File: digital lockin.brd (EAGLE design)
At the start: 76.2 x 94.9 mm, 24 parts, among them IC1 OPA2650E, IC2 LM358D, T2 NPN, U2 RASPBERRY_PICOSMD-TH, U5 TL431AIDBZR

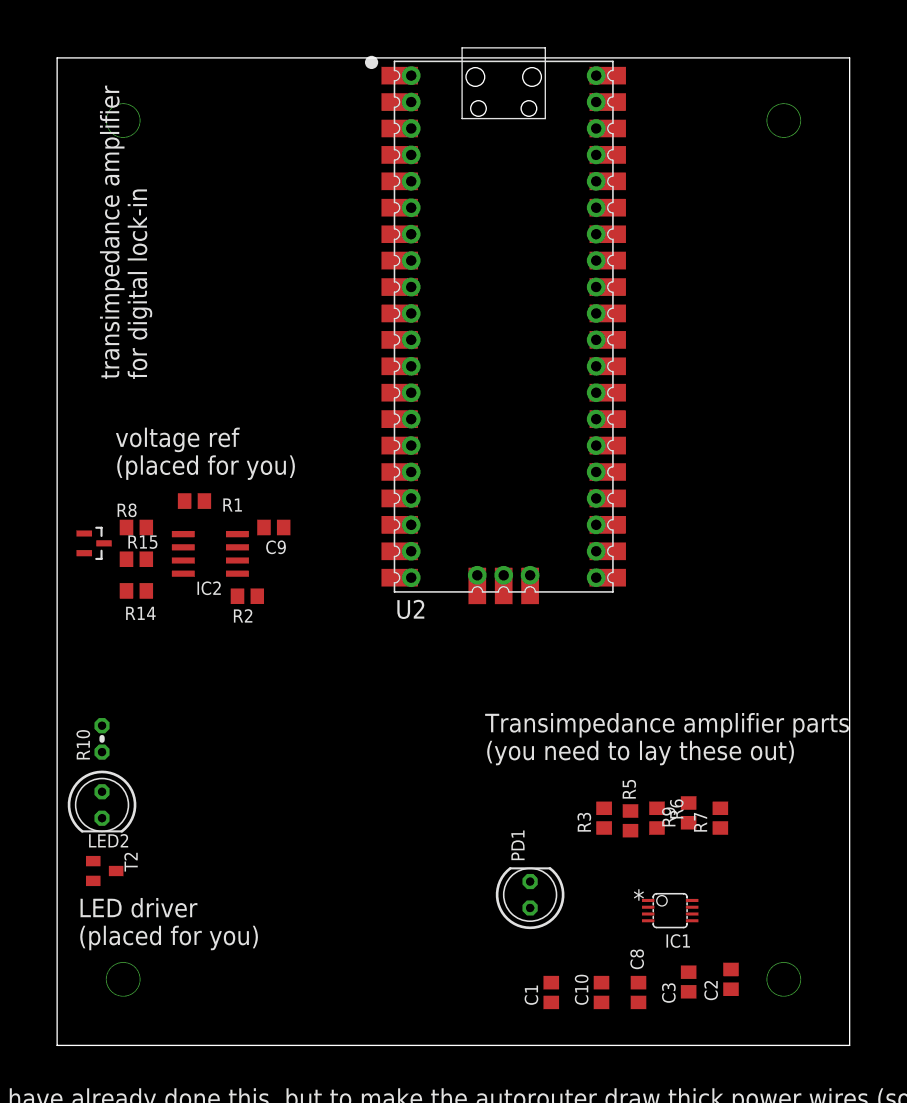
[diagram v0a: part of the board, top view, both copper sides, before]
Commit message: Lab 3 lock-in amplifier
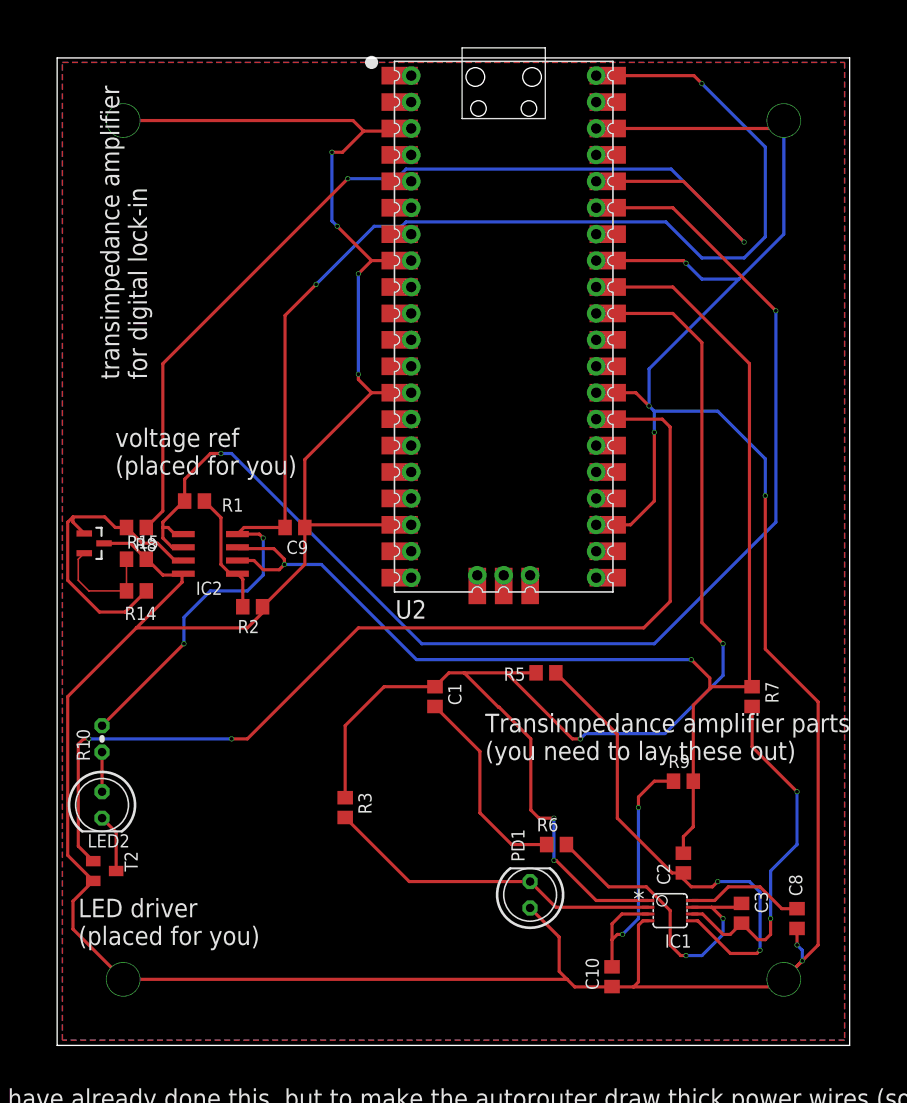
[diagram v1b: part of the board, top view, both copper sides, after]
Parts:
- moved C1 30.6 mm to (36.3, 33.5), turned to 270 degrees
- moved R3 24.9 mm to (27.7, 22.9), turned to 90 degrees
- moved C8 16.8 mm to (71.1, 12.2)
- moved R5 16.4 mm to (47.0, 35.8), turned to 0 degrees
- moved C2 12.1 mm to (60.2, 17.5)
- moved R7 12.1 mm to (66.8, 33.5), turned to 90 degrees
- moved R6 9.98 mm to (48.0, 19.3), turned to 0 degrees
- moved C3 8.33 mm to (65.8, 12.7), turned to 90 degrees
- moved R9 3.09 mm to (60.2, 25.4), turned to 180 degrees
- moved C9 2.03 mm to (22.9, 49.8)
- moved C10 1.83 mm to (53.3, 6.60)
- moved R2 1.14 mm to (18.8, 42.2)
- turned R8 to 0 degrees
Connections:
- removed net V+: IC1.8
- removed net V-: IC1.4
- new net N$1: C3.2, IC1.7, R6.2
- new net N$13: C10.2, IC1.3, R9.2
- new net N$2: C3.1, IC1.6, R7.1
- new net N$4: C2.2, IC1.5, R5.2
- new net N$6: C1.2, R6.1
- new net N$7: IC1.2, PD1.K, R3.1
- new net N$8: C8.2, IC1.8
- net ADCMID: now also C2.1, R7.2, R9.1
- net AMPOUT: now also C1.1, IC1.1, R3.2, R5.1
- net GND: now also C10.1, C8.1, IC1.4, PD1.A
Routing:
- net GND: track 0.00 -> 411.3 mm, vias 4 -> 14
- net 5V: track 0.00 -> 133.2 mm, vias 0 -> 4
- net AMPOUT: track 0.00 -> 129.6 mm, vias 0 -> 4
- net ADCMID: track 0.00 -> 125.9 mm, vias 0 -> 2
- net ADCREF: track 0.00 -> 122.0 mm, vias 0 -> 2
- net 3V3: track 0.00 -> 99.6 mm, vias 0 -> 2
- net LEDCTRL: track 0.00 -> 97.5 mm, vias 0 -> 2
- net N$4: track 0.00 -> 47.4 mm, vias 0 -> 2
- net N$2: track 0.00 -> 34.4 mm, vias 0 -> 2
- net N$7: track 0.00 -> 32.7 mm
- net N$9: track 0.00 -> 30.5 mm
- net N$1: track 0.00 -> 30.2 mm, vias 0 -> 2
- net N$13: track 0.00 -> 27.1 mm, vias 0 -> 2
- net N$6: track 0.00 -> 19.7 mm
- net N$10: track 0.00 -> 12.1 mm
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- added copper zone on layer 1, net GND
- added copper zone on layer 16, net GND
